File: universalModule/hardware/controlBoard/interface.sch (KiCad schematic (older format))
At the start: 4 parts, among them J4 ShoeAConnectors, J5 MOTOR_BUS, J6 MOTOR_BUS_ALT, J7 ShoeBConnectors

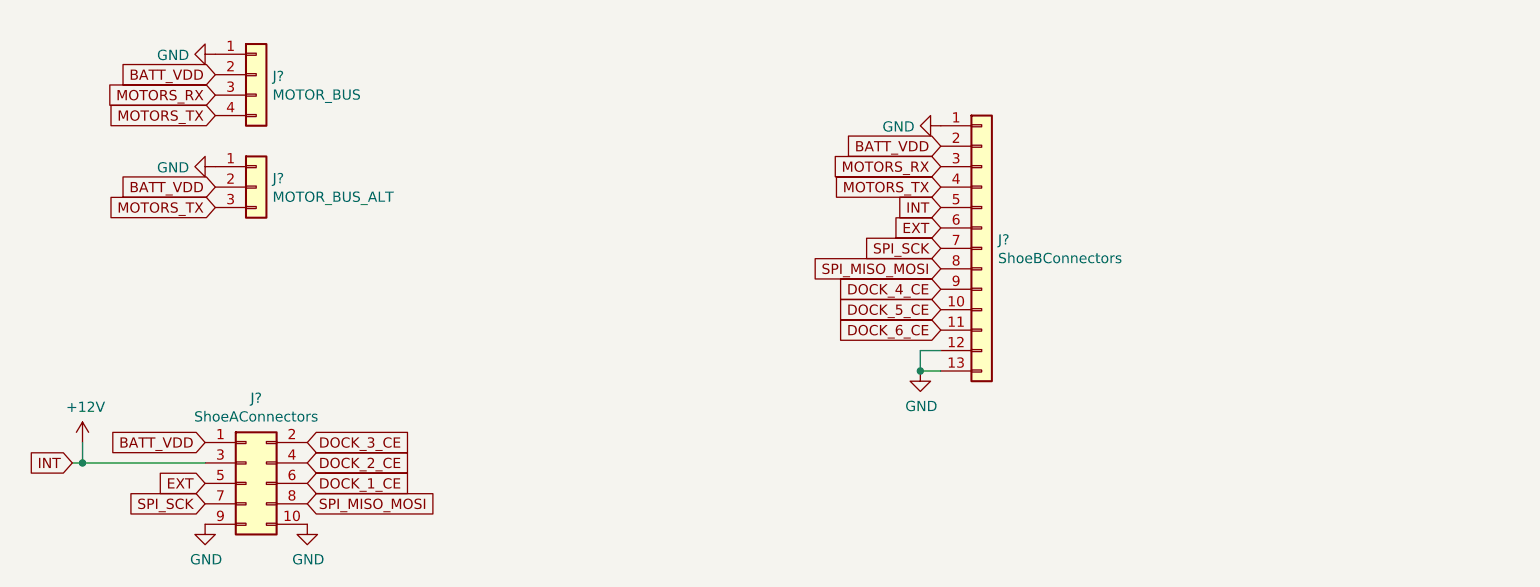
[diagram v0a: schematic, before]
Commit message: universalModule: Route the control boards
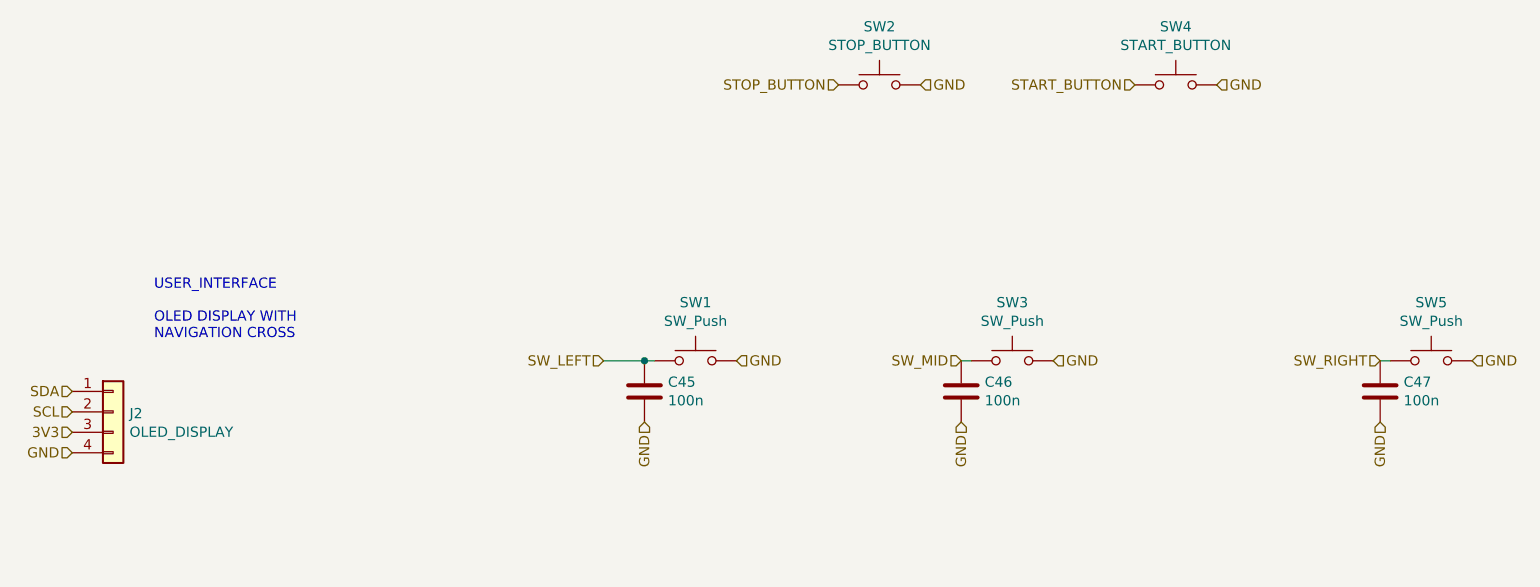
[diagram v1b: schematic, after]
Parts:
- removed J4: ShoeAConnectors, Connector_PinHeader_2.00mm:PinHeader_2x05_P2.00mm_Vertical, symbol Connector_Generic:Conn_02x05_Odd_Even
- removed J5: MOTOR_BUS, Connector_PinHeader_2.00mm:PinHeader_1x04_P2.00mm_Vertical, symbol Connector_Generic:Conn_01x04
- removed J6: MOTOR_BUS_ALT, Connector_PinHeader_2.00mm:PinHeader_1x03_P2.00mm_Vertical, symbol Connector_Generic:Conn_01x03
- removed J7: ShoeBConnectors, Connector_PinHeader_1.27mm:PinHeader_1x13_P1.27mm_Vertical, symbol Connector_Generic:Conn_01x13
- added C45, C46, C47: 100n, Capacitor_SMD:C_0402_1005Metric, symbol Device:C
- added J2: OLED_DISPLAY, rofi:OLED_128_32_I2C, symbol Connector_Generic:Conn_01x04
- added SW1, SW3, SW5: SW_Push, rofi:BUTTON_SMT_G_4_3, symbol Switch:SW_Push
- added SW2: STOP_BUTTON, rofi:BUTTON_SMT_G_4_3, symbol Switch:SW_Push
- added SW4: START_BUTTON, rofi:BUTTON_SMT_G_4_3, symbol Switch:SW_Push
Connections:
- net GND: now also C45.2, C46.2, C47.2, J2.4 (Pin_4), SW1.2, SW2.2, SW3.2, SW4.2, SW5.2
- new net 3V3: J2.3 (Pin_3)
- new net SCL: J2.2 (Pin_2)
- new net SDA: J2.1 (Pin_1)
- new net START_BUTTON: SW4.1
- new net STOP_BUTTON: SW2.1
- new net SW_LEFT: C45.1, SW1.1
- new net SW_MID: C46.1, SW3.1
- new net SW_RIGHT: C47.1, SW5.1
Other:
- note added: "USER_INTERFACE\n\nOLED DISPLAY WITH\nNAVIGATION CROSS"
